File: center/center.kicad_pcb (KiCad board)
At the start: 2 copper layers, 58.2 x 64 mm, 52 parts, among them J1 top left, J2 top right, J3 bottom right, J4 bottom left, J5 SWD, Q1 AO3400, Q2 IRLML6402, Q3 AO3400, Q4 AO3400, Q5 IRLML6402, U1 AP1117-33, U2 STM32F030F4P6, Y1 8MHz

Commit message: center: improve silk
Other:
- board text added: "+"
- board text added: "CK"
- board text added: "IO"
- board text added: "SWD"
- board text added: "github.com/ jaseg/8seg"
- board text added: "⏚"
- board text added: "▶"
- board text removed: "github.com/jaseg/8seg"
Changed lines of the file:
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@@
   (general
     (thickness 1.6)
-    (drawings 87)
+    (drawings 100)
     (tracks 363)
     (zones 0)
@@
   )
   (setup
-    (last_trace_width 1.2)
+    (last_trace_width 0.25)
     (user_trace_width 0.1)
     (user_trace_width 0.15)
@@
     (tags "capacitor 0805")
     (attr smd)
-    (fp_text reference C13 (at -0.04 1.59 90) (layer F.SilkS)
+    (fp_text reference C13 (at 2.6 -0.1 180) (layer F.SilkS)
       (effects (font (size 1 1) (thickness 0.15)))
     )
@@
     (tags "Diode SMB (DO-214AA) Handsoldering")
     (attr smd)
-    (fp_text reference D4 (at -0.168544 2.96752) (layer F.SilkS)
+    (fp_text reference D4 (at 3.771456 -2.16248) (layer F.SilkS)
       (effects (font (size 1 1) (thickness 0.15)))
     )
@@
     (tags "resistor 0603")
     (attr smd)
-    (fp_text reference R13 (at -1.49 1.43) (layer F.SilkS)
+    (fp_text reference R13 (at -0.3 2.6 90) (layer F.SilkS)
       (effects (font (size 1 1) (thickness 0.15)))
     )
@@
     (tags "resistor 0603")
     (attr smd)
-    (fp_text reference R14 (at 0 -1.45 90) (layer F.SilkS)
+    (fp_text reference R14 (at -3.55 -0.05 270) (layer F.SilkS)
       (effects (font (size 1 1) (thickness 0.15)))
     )
@@
     )
   )
-  (gr_text github.com/jaseg/8seg (at 98.71 115.46) (layer B.SilkS)
-    (effects (font (size 1.5 1.5) (thickness 0.3)) (justify mirror))
-  )
-  (gr_text cc-by-sa (at 82.09 105.76) (layer B.SilkS)
-    (effects (font (size 1.5 1.5) (thickness 0.3)) (justify mirror))
-  )
-  (gr_text "(c)2018 jaseg" (at 83.78 103.58) (layer B.SilkS)
-    (effects (font (size 1.5 1.5) (thickness 0.3)) (justify mirror))
-  )
-  (gr_text "8seg R01" (at 85.89 100.04) (layer B.SilkS)
-    (effects (font (size 3 3) (thickness 0.5)) (justify mirror))
+  (gr_text ▶ (at 101.7 84.75 270) (layer F.SilkS)
+    (effects (font (size 1.5 1.5) (thickness 0.3)))
+  )
+  (gr_text ▶ (at 85.55 103.3 180) (layer F.SilkS)
+    (effects (font (size 1.5 1.5) (thickness 0.3)))
+  )
+  (gr_text ▶ (at 85.6 99.95) (layer F.SilkS)
+    (effects (font (size 1.5 1.5) (thickness 0.3)))
+  )
+  (gr_text ▶ (at 108.45 95.7 90) (layer F.SilkS)
+    (effects (font (size 1.5 1.5) (thickness 0.3)))
+  )
+  (gr_text ▶ (at 112.05 88.65) (layer F.SilkS)
+    (effects (font (size 1.5 1.5) (thickness 0.3)))
+  )
+  (gr_text ▶ (at 112.05 83.65) (layer F.SilkS)
+    (effects (font (size 1.5 1.5) (thickness 0.3)))
+  )
+  (gr_text ▶ (at 88.15 88.8 180) (layer F.SilkS)
+    (effects (font (size 1.5 1.5) (thickness 0.3)))
+  )
+  (gr_text ▶ (at 88.1 83.75 180) (layer F.SilkS)
+    (effects (font (size 1.5 1.5) (thickness 0.3)))
+  )
+  (gr_text SWD (at 86.7 92.45) (layer F.SilkS)
+    (effects (font (size 1.5 1.5) (thickness 0.3)))
+  )
+  (gr_text ⏚ (at 85.65 94.6) (layer F.SilkS)
+    (effects (font (size 1.5 1.5) (thickness 0.3)))
+  )
+  (gr_text + (at 90.7 94.4) (layer F.SilkS)
+    (effects (font (size 1.5 1.5) (thickness 0.3)))
+  )
+  (gr_text CK (at 88.15 94.5) (layer F.SilkS)
+    (effects (font (size 1.5 1.5) (thickness 0.3)))
+  )
+  (gr_text IO (at 83.1 94.55) (layer F.SilkS)
+    (effects (font (size 1.5 1.5) (thickness 0.3)))
+  )
+  (gr_text "github.com/\njaseg/8seg" (at 79.4 124.75 323) (layer F.SilkS)
+    (effects (font (size 1.5 1.5) (thickness 0.3)))
+  )
+  (gr_text cc-by-sa (at 117.2 124.05 307) (layer F.SilkS)
+    (effects (font (size 1.5 1.5) (thickness 0.3)))
+  )
+  (gr_text "(c)2018 jaseg" (at 117.65 120.85 307) (layer F.SilkS)
+    (effects (font (size 1.5 1.5) (thickness 0.3)))
+  )
+  (gr_text "8seg R01" (at 119.95 118.5 307) (layer F.SilkS)
+    (effects (font (size 2.5 2.5) (thickness 0.4)))
   )
   (gr_text ↑UP↑ (at 99.65 78.02) (layer B.SilkS)
@@
   (gr_line (start 125 75) (end 125 125) (layer Dwgs.User) (width 0.2))
   (gr_line (start 75 75) (end 125 75) (layer Dwgs.User) (width 0.2))
-  (via (at 95.175 104.575) (size 2) (drill 1) (layers F.Cu B.Cu) (net 2))
   (segment (start 87 108.9) (end 85.8 110.1) (width 1.2) (layer F.Cu) (net 1))
   (segment (start 87 107.95) (end 87 108.9) (width 1.2) (layer F.Cu) (net 1))
@@
   (via (at 106.477354 78.44672) (size 2) (drill 1) (layers F.Cu B.Cu) (net 1))
   (via (at 99.5 77.5) (size 2) (drill 1) (layers F.Cu B.Cu) (net 1))
+  (via (at 95.175 104.575) (size 2) (drill 1) (layers F.Cu B.Cu) (net 2))
   (segment (start 105.5 101.025) (end 105.5 101.25) (width 0.3) (layer F.Cu) (net 2))
   (segment (start 104.8 100.325) (end 105.5 101.025) (width 0.3) (layer F.Cu) (net 2))

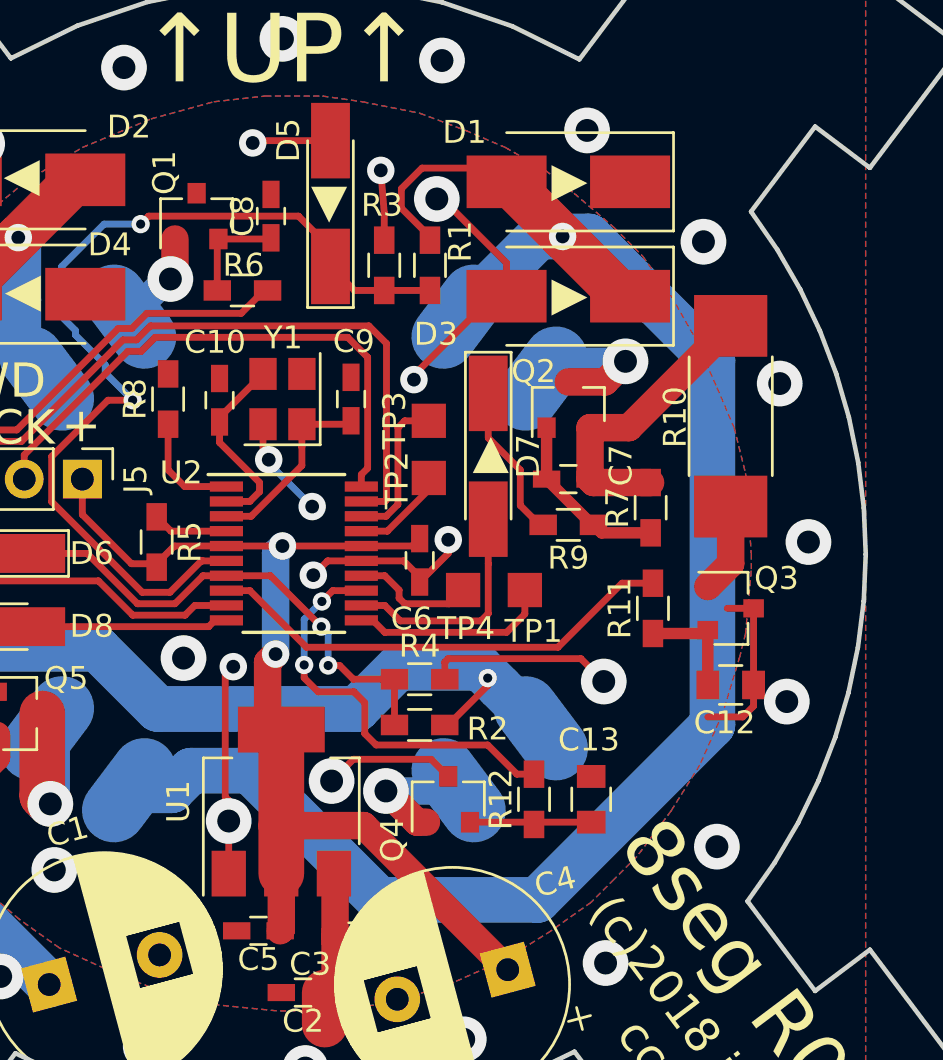
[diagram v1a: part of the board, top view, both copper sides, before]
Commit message: Fix AO3400 pinout
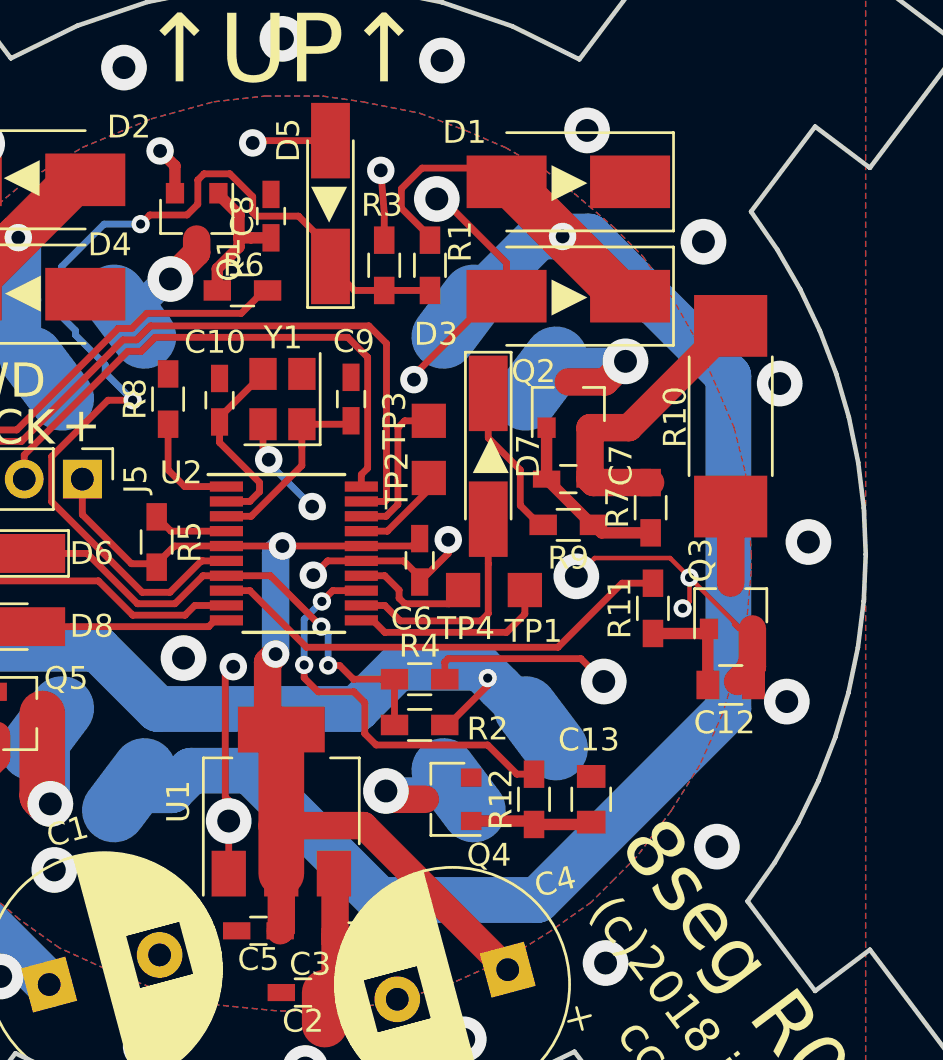
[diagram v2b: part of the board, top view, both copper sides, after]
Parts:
- Q2, Q5: value IRLML6402 -> AO3401
- moved Q3 0.10 mm to (119.1, 102.3), turned to 90 degrees
- turned Q1 to 270 degrees
- turned Q4 to 180 degrees
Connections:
- Q1 pad 1: /Q0 -> Net-(C8-Pad1)
- Q1 pad 2: Net-(C8-Pad1) -> GND
- Q1 pad 3: GND -> /Q0
- Q3 pad 1: Net-(Q3-Pad1) -> Net-(C12-Pad1)
- Q3 pad 2: Net-(C12-Pad1) -> GND
- Q3 pad 3: GND -> Net-(Q3-Pad3)
- Q4 pad 1: /Q1 -> Net-(C13-Pad1)
- Q4 pad 2: Net-(C13-Pad1) -> GND
- Q4 pad 3: GND -> /Q1
- R10 pad 2: Net-(Q3-Pad1) -> Net-(Q3-Pad3)
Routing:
- net Net-(Q3-Pad1): track 3.91 -> 0.00 mm
- net Net-(Q3-Pad3): track 0.00 -> 3.35 mm
- net GND: track 63.7 -> 67.0 mm, vias 15 -> 18
- net /Vmeas_A: track 42.3 -> 44.9 mm
- net Net-(C8-Pad1): track 4.59 -> 6.49 mm
- net /Q0: track 4.32 -> 4.99 mm
- net Net-(D1-Pad2): track 77.6 -> 78.1 mm
